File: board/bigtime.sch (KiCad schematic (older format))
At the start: 61 parts, among them IC1 NPIC6C596A, IC2 TPS62152, IC3 25AA02E48, IC4 STM32F407VET6, IC8 LDL212DR, J2 MICROUSB, P1 CONN_IN, P2 CONN_OUT, P3 +12V, P4 SWD_TC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

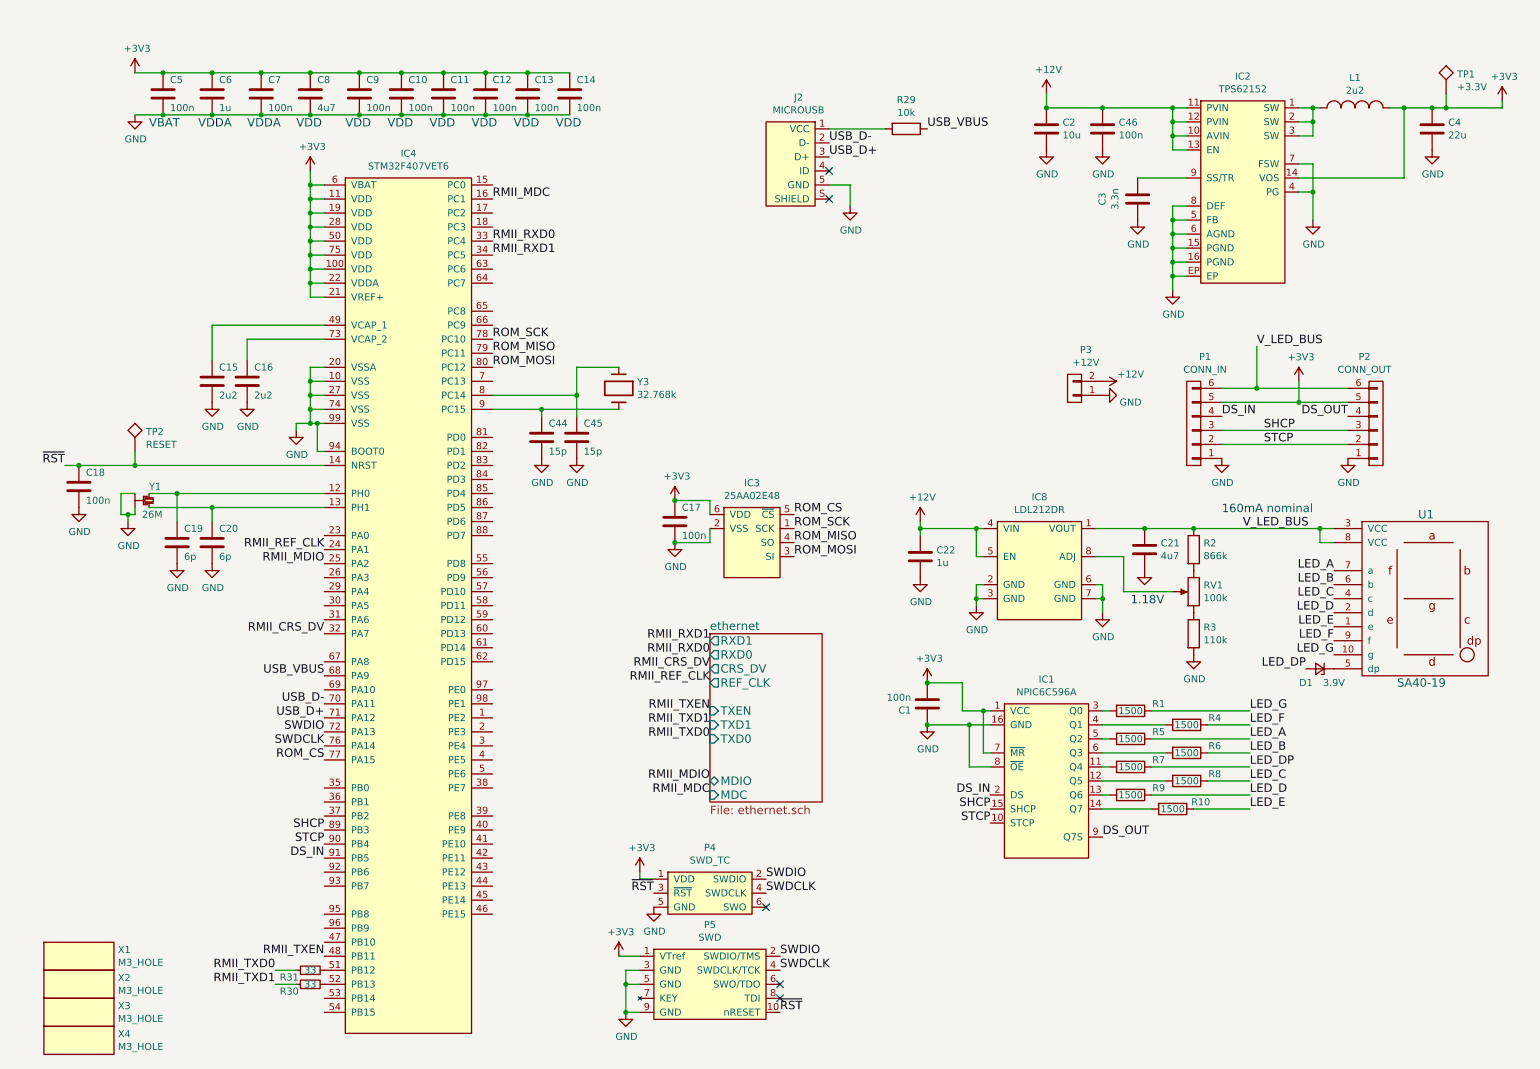
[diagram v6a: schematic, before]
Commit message: Fixed ERC with liberal application of pwr_flag
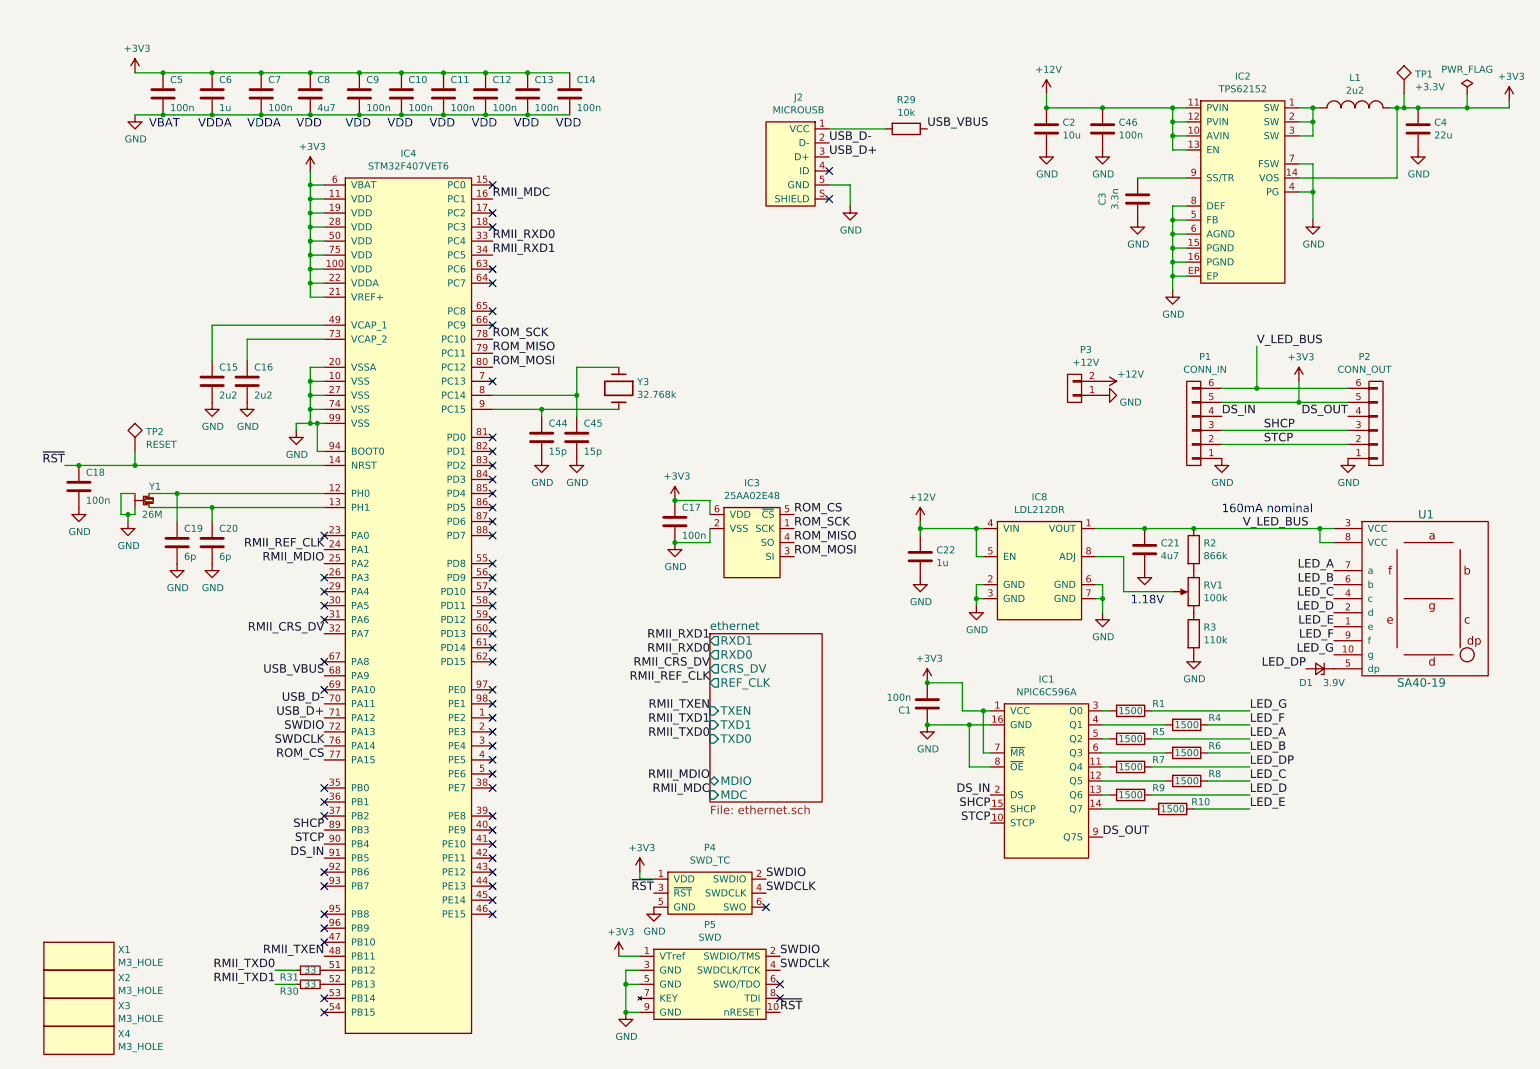
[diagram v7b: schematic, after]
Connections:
- no-connect marks 5 -> 62
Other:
- moved on the sheet: C4, TP1
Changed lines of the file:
@@
 L C C4
 U 1 1 58AB75BC
-P 10450 1150
-F 0 "C4" H 10565 1196 50  0000 L CNN
-F 1 "22u" H 10565 1105 50  0000 L CNN
-F 2 "agg:0603" H 1988 -200 50  0001 C CNN
-F 3 "" H 1950 -50 50  0000 C CNN
-F 4 "2494232" H 10450 1150 60  0001 C CNN "Farnell"
-	1    10450 1150
+P 10350 1150
+F 0 "C4" H 10465 1196 50  0000 L CNN
+F 1 "22u" H 10465 1105 50  0000 L CNN
+F 2 "agg:0603" H 1888 -200 50  0001 C CNN
+F 3 "" H 1850 -50 50  0000 C CNN
+F 4 "2494232" H 10350 1150 60  0001 C CNN "Farnell"
+	1    10350 1150
 	1    0    0    -1
 $EndComp
@@
 L +3V3 #PWR08
 U 1 1 58AB765A
-P 10950 950
-F 0 "#PWR08" H 11000 1000 50  0001 C CNN
-F 1 "+3V3" H 10965 1123 50  0000 C CNN
-F 2 "" H 2150 -150 50  0000 C CNN
-F 3 "" H 2150 -150 50  0000 C CNN
-	1    10950 950
+P 11000 950
+F 0 "#PWR08" H 11050 1000 50  0001 C CNN
+F 1 "+3V3" H 11015 1123 50  0000 C CNN
+F 2 "" H 2200 -150 50  0000 C CNN
+F 3 "" H 2200 -150 50  0000 C CNN
+	1    11000 950
 	1    0    0    -1
 $EndComp
@@
 L GND #PWR09
 U 1 1 58AB76DE
-P 10450 1300
-F 0 "#PWR09" H 2350 -500 50  0001 C CNN
-F 1 "GND" H 10455 1127 50  0000 C CNN
-F 2 "" H 2350 -250 50  0000 C CNN
-F 3 "" H 2350 -250 50  0000 C CNN
-	1    10450 1300
+P 10350 1300
+F 0 "#PWR09" H 2250 -500 50  0001 C CNN
+F 1 "GND" H 10355 1127 50  0000 C CNN
+F 2 "" H 2250 -250 50  0000 C CNN
+F 3 "" H 2250 -250 50  0000 C CNN
+	1    10350 1300
 	1    0    0    -1
 $EndComp
@@
 Connection ~ 9600 1100
 Wire Wire Line
-	10150 1000 10950 1000
-Wire Wire Line
-	10250 1000 10250 1500
-Wire Wire Line
-	10250 1500 9500 1500
-Connection ~ 10250 1000
-Wire Wire Line
-	10950 1000 10950 950
-Connection ~ 10450 1000
+	10150 1000 11000 1000
+Wire Wire Line
+	10200 1000 10200 1500
+Wire Wire Line
+	10200 1500 9500 1500
+Connection ~ 10200 1000
+Wire Wire Line
+	11000 1000 11000 950
+Connection ~ 10350 1000
 Wire Wire Line
 	8350 1500 8700 1500
@@
 L TEST-RESCUE-bigtime TP1
 U 1 1 58D6D0D0
-P 10550 900
-F 0 "TP1" H 10628 1040 50  0000 L CNN
-F 1 "+3.3V" H 10628 949 50  0000 L CNN
-F 2 "agg:SIL-254P-01" H 10550 900 50  0001 C CNN
-F 3 "" H 10550 900 50  0001 C CNN
-	1    10550 900
-	1    0    0    -1
-$EndComp
-Wire Wire Line
-	10550 900  10550 1000
-Connection ~ 10550 1000
+P 10250 900
+F 0 "TP1" H 10328 1040 50  0000 L CNN
+F 1 "+3.3V" H 10328 949 50  0000 L CNN
+F 2 "agg:SIL-254P-01" H 10250 900 50  0001 C CNN
+F 3 "" H 10250 900 50  0001 C CNN
+	1    10250 900
+	1    0    0    -1
+$EndComp
 $Comp
 L TEST-RESCUE-bigtime TP2
@@
 Text Label 9150 5700 0    60   ~ 0
 LED_DP
+NoConn ~ 3750 1550
+NoConn ~ 3750 1750
+NoConn ~ 3750 1850
+NoConn ~ 3750 2150
+NoConn ~ 3750 2250
+NoConn ~ 3750 2450
+NoConn ~ 3750 2950
+NoConn ~ 3750 3350
+NoConn ~ 3750 3450
+NoConn ~ 3750 3550
+NoConn ~ 3750 3650
+NoConn ~ 3750 3750
+NoConn ~ 3750 3850
+NoConn ~ 3750 3950
+NoConn ~ 3750 4050
+NoConn ~ 3750 4250
+NoConn ~ 3750 4350
+NoConn ~ 3750 4450
+NoConn ~ 3750 4550
+NoConn ~ 3750 4650
+NoConn ~ 3750 4750
+NoConn ~ 3750 4850
+NoConn ~ 3750 4950
+NoConn ~ 3750 5150
+NoConn ~ 3750 5250
+NoConn ~ 3750 5350
+NoConn ~ 3750 5450
+NoConn ~ 3750 5550
+NoConn ~ 3750 5650
+NoConn ~ 3750 5750
+NoConn ~ 3750 5850
+NoConn ~ 3750 6050
+NoConn ~ 3750 6150
+NoConn ~ 3750 6250
+NoConn ~ 3750 6350
+NoConn ~ 3750 6450
+NoConn ~ 3750 6550
+NoConn ~ 3750 6650
+NoConn ~ 3750 6750
+NoConn ~ 2550 4050
+NoConn ~ 2550 4350
+NoConn ~ 2550 4450
+NoConn ~ 2550 4550
+NoConn ~ 2550 4650
+NoConn ~ 2550 4950
+NoConn ~ 2550 5150
+NoConn ~ 2550 5850
+NoConn ~ 2550 5950
+NoConn ~ 2550 6050
+NoConn ~ 2550 6450
+NoConn ~ 2550 6550
+NoConn ~ 2550 6750
+NoConn ~ 2550 6850
+NoConn ~ 2550 6950
+NoConn ~ 2550 7350
+NoConn ~ 2550 7450
+NoConn ~ 3750 2550
+Wire Wire Line
+	10250 900  10250 1000
+Connection ~ 10250 1000
+$Comp
+L PWR_FLAG #FLG041
+U 0 1 58E0C1AE
+P 10700 900
+F 0 "#FLG041" H 10700 975 50  0001 C CNN
+F 1 "PWR_FLAG" H 10700 1074 50  0000 C CNN
+F 2 "" H 10700 900 50  0001 C CNN
+F 3 "" H 10700 900 50  0001 C CNN
+	0    10700 900
+	1    0    0    -1
+$EndComp
+Wire Wire Line
+	10700 900  10700 1000
+Connection ~ 10700 1000
 $EndSCHEMATC

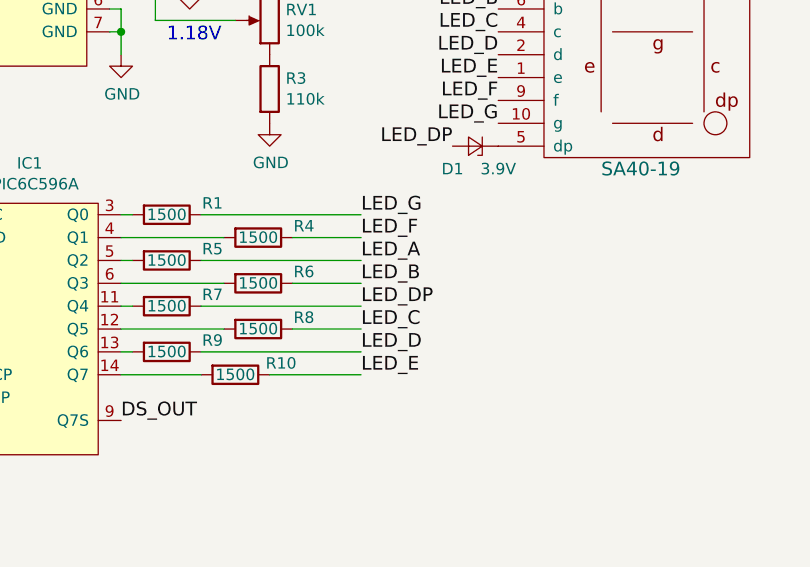
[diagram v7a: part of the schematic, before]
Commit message: Finished cleaning routing, rounded corners
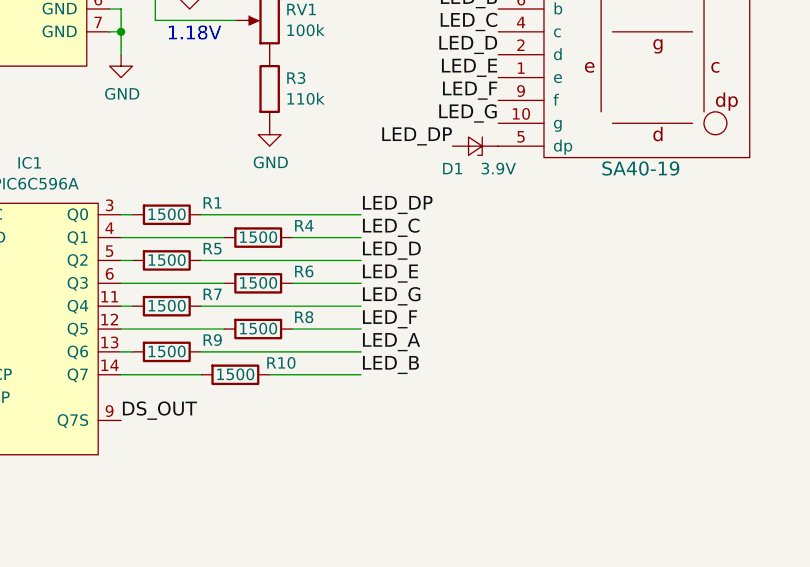
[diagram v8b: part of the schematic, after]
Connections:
- net LED_A: now also R9.1; no longer R5.1
- net LED_B: now also R10.1; no longer R6.1
- net LED_C: now also R4.1; no longer R8.1
- net LED_D: now also R5.1; no longer R9.1
- net LED_DP: now also R1.1; no longer R7.1
- net LED_E: now also R6.1; no longer R10.1
- net LED_F: now also R8.1; no longer R4.1
- net LED_G: now also R7.1; no longer R1.1
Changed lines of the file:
@@
 Text Label 9550 5000 2    60   ~ 0
 LED_DP
+Text Label 9150 6000 0    60   ~ 0
+LED_B
+Text Label 9150 5900 0    60   ~ 0
+LED_A
+Text Label 9150 5800 0    60   ~ 0
+LED_F
+Text Label 9150 5700 0    60   ~ 0
+LED_G
 Text Label 9150 5600 0    60   ~ 0
-LED_B
+LED_E
 Text Label 9150 5500 0    60   ~ 0
-LED_A
+LED_D
 Text Label 9150 5400 0    60   ~ 0
-LED_F
+LED_C
 Text Label 9150 5300 0    60   ~ 0
-LED_G
-Text Label 9150 6000 0    60   ~ 0
-LED_E
-Text Label 9150 5900 0    60   ~ 0
-LED_D
-Text Label 9150 5800 0    60   ~ 0
-LED_C
-Text Label 9150 5700 0    60   ~ 0
 LED_DP
 NoConn ~ 3750 1550
